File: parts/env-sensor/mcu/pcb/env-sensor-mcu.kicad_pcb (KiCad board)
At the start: 2 copper layers, 53.3 x 33 mm, 9 parts, among them J1 Conn_02x08_Top_Bottom, J2 Conn_02x08_Top_Bottom, J3 Conn_01x01_Shielded

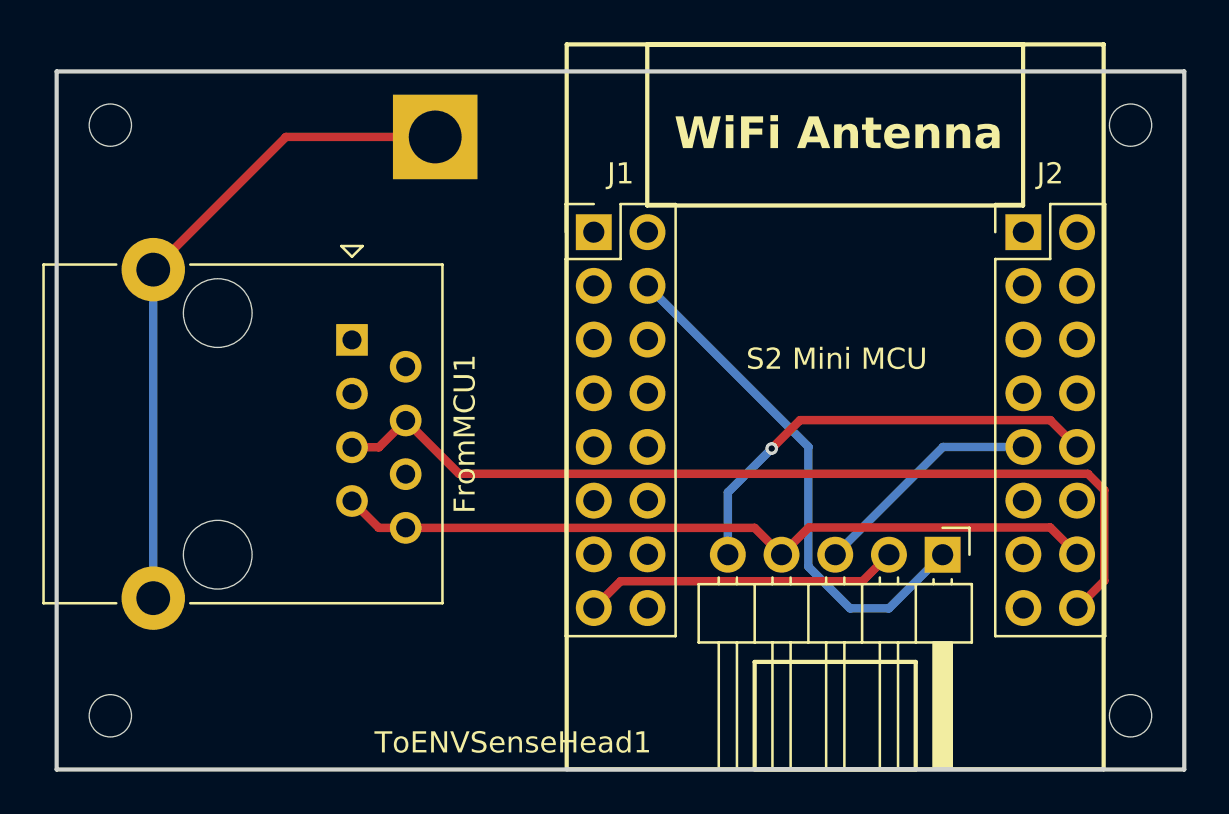
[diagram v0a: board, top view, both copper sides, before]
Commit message: 1.4.2 scoot mcu pad over to allow more clearance for standoff posts
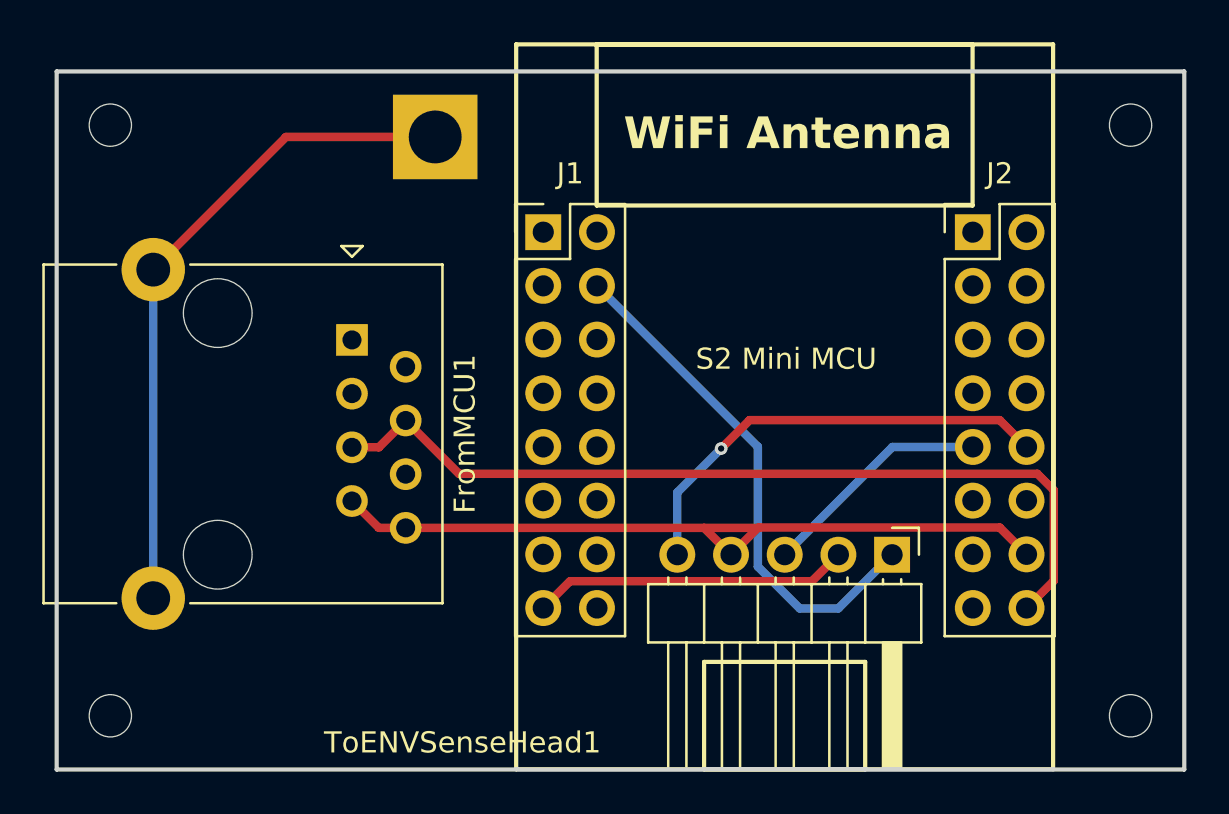
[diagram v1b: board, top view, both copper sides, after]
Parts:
- moved J1 2.39 mm to (66.2, 116.8)
- moved J2 2.39 mm to (86.6, 116.8)
- moved ToENVSenseHead1 2.39 mm to (80.2, 132.1)
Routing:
- net /5V: track 43.6 -> 41.2 mm
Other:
- board text added: "(C) 2026 ARKADIA HOUSE Env Sensor MCU rev 1.4.2"
- board text removed: "(C) 2026 ARKADIA HOUSE Env Sensor MCU rev 1.4.1"
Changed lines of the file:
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@@
 	(footprint "Connector_PinSocket_2.54mm:PinSocket_2x08_P2.54mm_Vertical"
 		(layer "F.Cu")
-		(at 88.9596 116.8225)
+		(at 86.5688 116.8225)
 		(descr "Through hole straight socket strip, 2x08, 2.54mm pitch, double cols (from Kicad 4.0.7), script generated")
 		(tags "Through hole socket strip THT 2x08 2.54mm double row")
@@
 	(footprint "Connector_PinSocket_2.54mm:PinSocket_2x08_P2.54mm_Vertical"
 		(layer "F.Cu")
-		(at 68.6396 116.8225)
+		(at 66.2488 116.8225)
 		(descr "Through hole straight socket strip, 2x08, 2.54mm pitch, double cols (from Kicad 4.0.7), script generated")
 		(tags "Through hole socket strip THT 2x08 2.54mm double row")
@@
 	(footprint "Connector_PinHeader_2.54mm:PinHeader_1x05_P2.54mm_Horizontal"
 		(layer "F.Cu")
-		(at 82.55 132.08 -90)
+		(at 80.1592 132.08 -90)
 		(descr "Through hole angled pin header, 1x05, 2.54mm pitch, 6mm pin length, single row")
 		(tags "Through hole angled pin header THT 1x05 2.54mm single row")
@@
 	(gr_poly
 		(pts
-			(xy 64.76713 107.940296) (xy 90.167132 107.940296) (xy 90.167134 142.230294) (xy 64.767133 142.230296)
+			(xy 62.37633 107.940296) (xy 87.776332 107.940296) (xy 87.776334 142.230294) (xy 62.376333 142.230296)
 		)
 		(stroke
@@
 	(gr_poly
 		(pts
-			(xy 68.57713 107.940298) (xy 86.357132 107.940293) (xy 86.357133 115.560296) (xy 68.577131 115.560292)
+			(xy 66.18633 107.940298) (xy 83.966332 107.940293) (xy 83.966333 115.560296) (xy 66.186331 115.560292)
 		)
 		(stroke
@@
 	(gr_poly
 		(pts
-			(xy 73.657135 137.150293) (xy 81.277129 137.150298) (xy 81.277133 142.230294) (xy 73.657134 142.230296)
+			(xy 71.266335 137.150293) (xy 78.886329 137.150298) (xy 78.886333 142.230294) (xy 71.266334 142.230296)
 		)
 		(stroke
@@
 	)
 	(gr_text "S2 Mini MCU"
-		(at 77.540957 122.8212 0)
+		(at 75.150157 122.8212 0)
 		(layer "F.SilkS")
 		(effects
@@
 	)
 	(gr_text "WiFi Antenna"
-		(at 69.85 113.03 0)
+		(at 67.4592 113.03 0)
 		(layer "F.SilkS")
 		(effects
@@
 	)
 	(gr_text "ILL 3V3 SDA GND SCL\n"
-		(at 83.1088 134.5438 0)
+		(at 80.718 134.5438 0)
 		(layer "B.SilkS")
 		(effects
@@
 	)
 	(gr_text "for Linda"
-		(at 82.980992 111.412215 0)
+		(at 80.590192 111.412215 0)
 		(layer "B.SilkS")
 		(effects
@@
 		)
 	)
-	(gr_text "(C) 2026 ARKADIA HOUSE\nEnv Sensor MCU rev 1.4.1"
+	(gr_text "(C) 2026 ARKADIA HOUSE\nEnv Sensor MCU rev 1.4.2"
 		(at 75.438 141.040261 0)
 		(layer "B.SilkS")
@@
 	)
 	(barcode
-		(at 77.7278 116.7676 0)
+		(at 75.337 116.7676 0)
 		(layer "B.SilkS")
 		(size 10 10)
@@
 	)
 	(segment
-		(start 77.47 132.08)
-		(end 82.5675 126.9825)
+		(start 75.0792 132.08)
+		(end 80.1767 126.9825)
 		(width 0.4)
 		(layer "B.Cu")
@@
 	)
 	(segment
-		(start 82.5675 126.9825)
-		(end 86.3688 126.9825)
+		(start 80.1767 126.9825)
+		(end 83.978 126.9825)
 		(width 0.4)
 		(layer "B.Cu")
@@
 	)
 	(segment
-		(start 74.4639 127.0569)
-		(end 75.8083 125.7125)
+		(start 72.0731 127.0569)
+		(end 73.4175 125.7125)
 		(width 0.4)
 		(layer "F.Cu")
@@
 	)
 	(segment
-		(start 75.8083 125.7125)
-		(end 87.6388 125.7125)
+		(start 73.4175 125.7125)
+		(end 85.248 125.7125)
 		(width 0.4)
 		(layer "F.Cu")
@@
 	)
 	(segment
-		(start 87.6388 125.7125)
-		(end 88.9088 126.9825)
+		(start 85.248 125.7125)
+		(end 86.518 126.9825)
 		(width 0.4)
 		(layer "F.Cu")
@@
 	)
 	(via
-		(at 74.4639 127.0569)
+		(at 72.0731 127.0569)
 		(size 0.6)
 		(drill 0.3)
@@
 	)
 	(segment
-		(start 72.39 132.08)
-		(end 72.39 129.1308)
+		(start 69.9992 132.08)
+		(end 69.9992 129.1308)
 		(width 0.4)
 		(layer "B.Cu")
@@
 	)
 	(segment
-		(start 72.39 129.1308)
-		(end 74.4639 127.0569)
+		(start 69.9992 129.1308)
+		(end 72.0731 127.0569)
 		(width 0.4)
 		(layer "B.Cu")
@@
 	)
 	(segment
-		(start 76.2175 130.7925)
-		(end 87.6388 130.7925)
+		(start 73.8267 130.7925)
+		(end 85.248 130.7925)
 		(width 0.4)
 		(layer "F.Cu")
@@
 	)
 	(segment
-		(start 87.6388 130.7925)
-		(end 88.9088 132.0625)
+		(start 85.248 130.7925)
+		(end 86.518 132.0625)
 		(width 0.4)
 		(layer "F.Cu")
@@
 	)
 	(segment
-		(start 74.93 132.08)
-		(end 76.2175 130.7925)
+		(start 72.5392 132.08)
+		(end 73.8267 130.7925)
 		(width 0.4)
 		(layer "F.Cu")
@@
 	)
 	(segment
-		(start 73.66 130.81)
-		(end 74.93 132.08)
+		(start 71.2692 130.81)
+		(end 72.5392 132.08)
 		(width 0.4)
 		(layer "F.Cu")
@@
 	)
 	(segment
-		(start 89.4214 128.2525)
-		(end 90.1986 129.0297)
+		(start 87.0306 128.2525)
+		(end 87.8078 129.0297)
 		(width 0.4)
 		(layer "F.Cu")
@@
 	)
 	(segment
-		(start 90.1986 129.0297)
-		(end 90.1986 133.3127)
-		(width 0.4)
-		(layer "F.Cu")
-		(net "/5V")
-	)
-	(segment
-		(start 90.1986 133.3127)
-		(end 88.9088 134.6025)
-		(width 0.4)
-		(layer "F.Cu")
-		(net "/5V")
-	)
-	(segment
-		(start 59.6725 128.2525)
-		(end 89.4214 128.2525)
+		(start 87.8078 129.0297)
+		(end 87.8078 133.3127)
 		(width 0.4)
 		(layer "F.Cu")
@@
 	)
 	(segment
+		(start 87.8078 133.3127)
+		(end 86.518 134.6025)
+		(width 0.4)
+		(layer "F.Cu")
+		(net "/5V")
+	)
+	(segment
+		(start 59.6725 128.2525)
+		(end 87.0306 128.2525)
+		(width 0.4)
+		(layer "F.Cu")
+		(net "/5V")
+	)
+	(segment
 		(start 54.61 127)
 		(end 55.88 127)
@@
 	)
 	(segment
-		(start 78.1747 134.62)
-		(end 80.01 134.62)
+		(start 75.7839 134.62)
+		(end 77.6192 134.62)
 		(width 0.4)
 		(layer "B.Cu")
@@
 	)
 	(segment
-		(start 76.2 132.6453)
-		(end 78.1747 134.62)
+		(start 73.8092 132.6453)
+		(end 75.7839 134.62)
 		(width 0.4)
 		(layer "B.Cu")
@@
 	)
 	(segment
-		(start 76.2 126.9737)
-		(end 76.2 132.6453)
+		(start 73.8092 126.9737)
+		(end 73.8092 132.6453)
 		(width 0.4)
 		(layer "B.Cu")
@@
 	)
 	(segment
-		(start 80.01 134.62)
-		(end 82.55 132.08)
+		(start 77.6192 134.62)
+		(end 80.1592 132.08)
 		(width 0.4)
 		(layer "B.Cu")
@@
 	)
 	(segment
-		(start 68.5888 119.3625)
-		(end 76.2 126.9737)
+		(start 66.198 119.3625)
+		(end 73.8092 126.9737)
 		(width 0.4)
 		(layer "B.Cu")
@@
 	)
 	(segment
-		(start 67.3187 133.3326)
-		(end 78.7574 133.3326)
+		(start 64.9279 133.3326)
+		(end 76.3666 133.3326)
 		(width 0.4)
 		(layer "F.Cu")
@@
 	)
 	(segment
-		(start 78.7574 133.3326)
-		(end 80.01 132.08)
+		(start 76.3666 133.3326)
+		(end 77.6192 132.08)
 		(width 0.4)
 		(layer "F.Cu")
@@
 	)
 	(segment
-		(start 66.0488 134.6025)
-		(end 67.3187 133.3326)
-		(width 0.4)
-		(layer "F.Cu")
+		(start 63.658 134.6025)
+		(end 64.9279 133.3326)
+		(width 0.4)
+		(layer "F.Cu")
